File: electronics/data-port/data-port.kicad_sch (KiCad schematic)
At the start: 0 parts

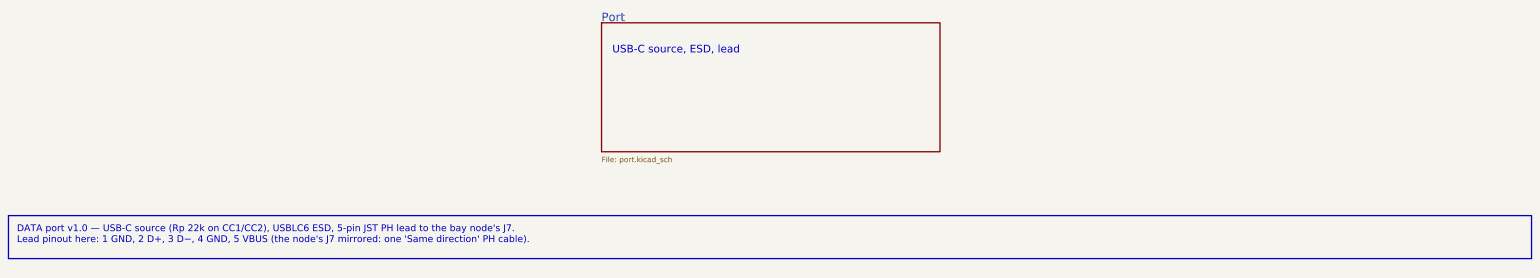
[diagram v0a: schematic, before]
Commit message: DATA lead on 8 wires: node J7 a vertical PH 8 (USB, I²C, INT), data port J2 an S8B
Density decisions of 2026-10-19: the DATA lead becomes the camera's PH 8
"Same direction" type and also carries the node's I²C and an open-drain,
active-low INT (IO4, 10k pull-up, 1k at J7) for a later DATA ×4 board.

- Node: J7 B8B vertical by the right edge (J5's old slot), J5 AUX
  horizontal in the middle, AUX parts in a column between them.  J7 now
  taps the pair at J4's pads (DUT_CONN_*, behind U8's ESD like J4); the
  branch is hand-drawn in usb_hs_routes() on B.Cu under J4, since
  Freerouting found no room on U8's mux side.  ERC 0, DRC 0, parity 0,
  99 models.
- Data port: S8B, pins 1–3 open, PH at x 14.4, left hole (2.6, 13.5),
  one silkscreen label per pin.  ERC 0, DRC 0, parity 0.
- Pin map (README, check_pinmap: DATA_INT reserved), docs, cabling,
  BOM (one PH 8 lead type for DATA and camera, no B5B/S5B), SCAD config.

Co-Authored-By: Claude Opus 5.5 <noreply@anthropic.com>
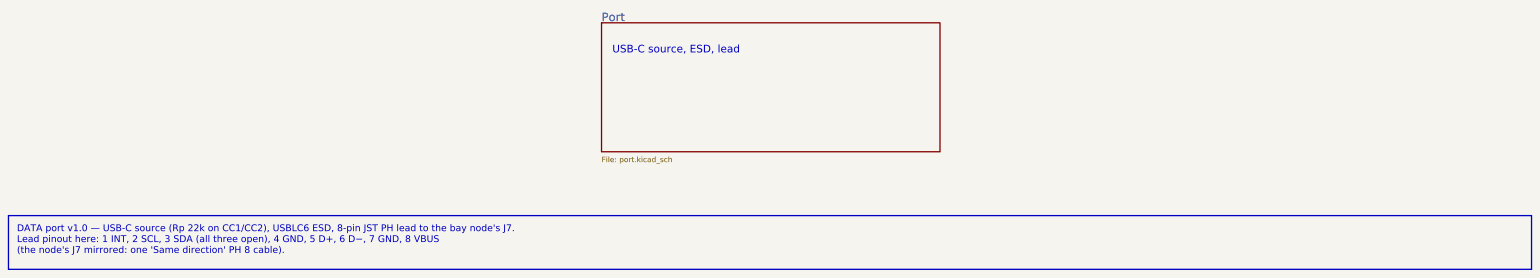
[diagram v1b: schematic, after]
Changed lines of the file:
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@@
 		)
 	)
-	(text_box "DATA port v1.0 — USB-C source (Rp 22k on CC1/CC2), USBLC6 ESD, 5-pin JST PH lead to the bay node's J7.\nLead pinout here: 1 GND, 2 D+, 3 D−, 4 GND, 5 VBUS (the node's J7 mirrored: one 'Same direction' PH cable)."
+	(text_box "DATA port v1.0 — USB-C source (Rp 22k on CC1/CC2), USBLC6 ESD, 8-pin JST PH lead to the bay node's J7.\nLead pinout here: 1 INT, 2 SCL, 3 SDA (all three open), 4 GND, 5 D+, 6 D−, 7 GND, 8 VBUS\n  (the node's J7 mirrored: one 'Same direction' PH 8 cable)."
 		(exclude_from_sim no)
 		(at 30 115.57 0)
-		(size 360 10.16)
+		(size 360 12.7)
 		(margins 2 2 2 2)
 		(stroke

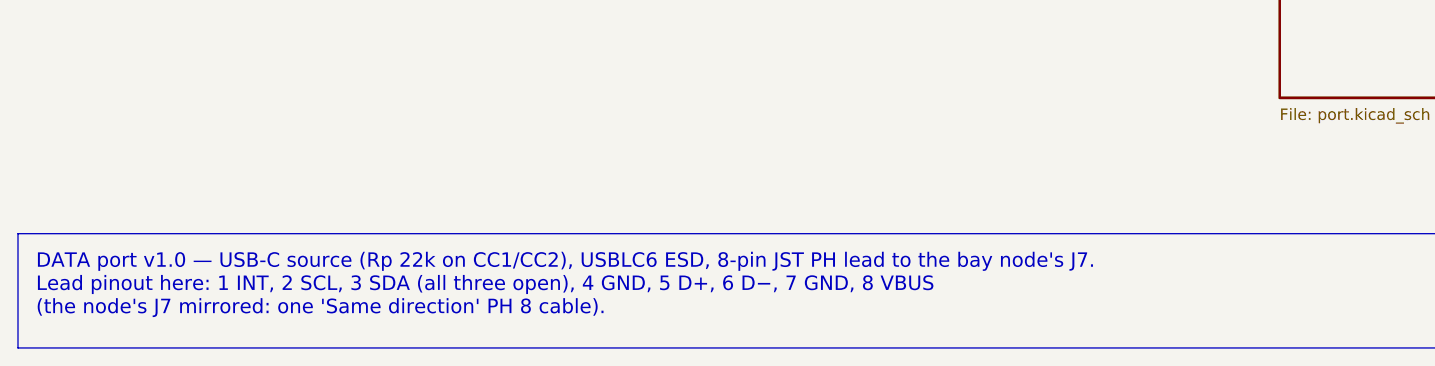
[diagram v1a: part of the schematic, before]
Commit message: Bay node: J7 takes D+ on pin 3, the DUT pair runs straight
U8 puts D- to the north and J7's side entry put D+ there, so D+ crossed
under D- on B.Cu.  The user chose to swap J7's pins 3/4 (3 D+, 4 D-):
DUT_CONN_DP/DN now run straight from U8 into J7, one 45° step each, no
via (14.6 / 14.7 mm; J3 -> J7 matched to ≈ 0.3 mm).

The data port follows through the lead (pin n <-> 9-n): J2 5 D-, 6 D+,
and U1's channels swap with it (D+ through 1/6), so every pad keeps the
copper it had.  Both boards re-routed: ERC 0, DRC 0, 0 unconnected,
parity 0, JLC READY.

The node's buck GND and +5V islands and the LDO tab are now exclusive
(0.5 mm), as on the hub: Freerouting cut buck-5v, then C12 off the LDO
tab.  Docs: electronics (HS path, J7 and lead pinouts), cabling, the
third Konnect round; BOM note.

Co-Authored-By: Claude Opus 5.5 <noreply@anthropic.com>
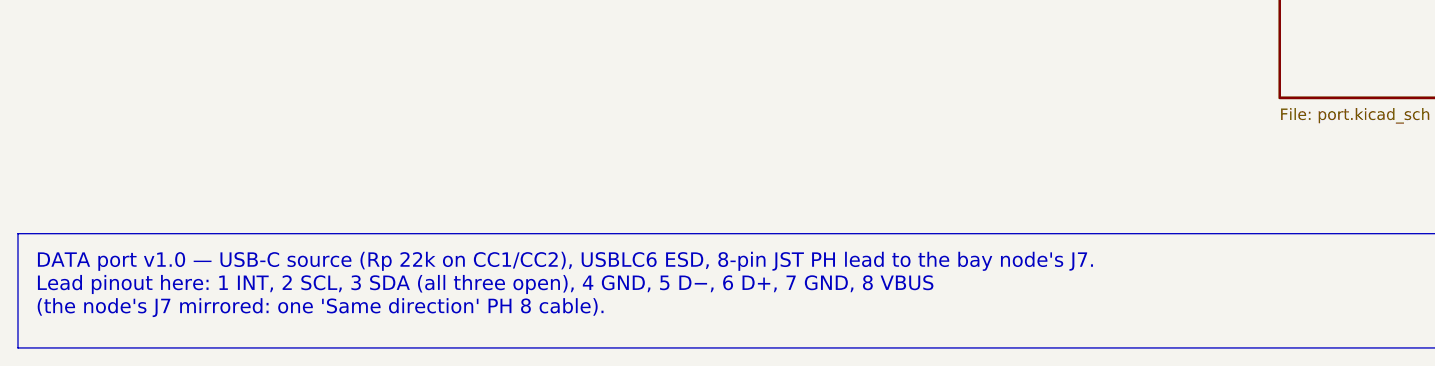
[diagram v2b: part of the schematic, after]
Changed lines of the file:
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@@
 		)
 	)
-	(text_box "DATA port v1.0 — USB-C source (Rp 22k on CC1/CC2), USBLC6 ESD, 8-pin JST PH lead to the bay node's J7.\nLead pinout here: 1 INT, 2 SCL, 3 SDA (all three open), 4 GND, 5 D+, 6 D−, 7 GND, 8 VBUS\n  (the node's J7 mirrored: one 'Same direction' PH 8 cable)."
+	(text_box "DATA port v1.0 — USB-C source (Rp 22k on CC1/CC2), USBLC6 ESD, 8-pin JST PH lead to the bay node's J7.\nLead pinout here: 1 INT, 2 SCL, 3 SDA (all three open), 4 GND, 5 D−, 6 D+, 7 GND, 8 VBUS\n  (the node's J7 mirrored: one 'Same direction' PH 8 cable)."
 		(exclude_from_sim no)
 		(at 30 115.57 0)

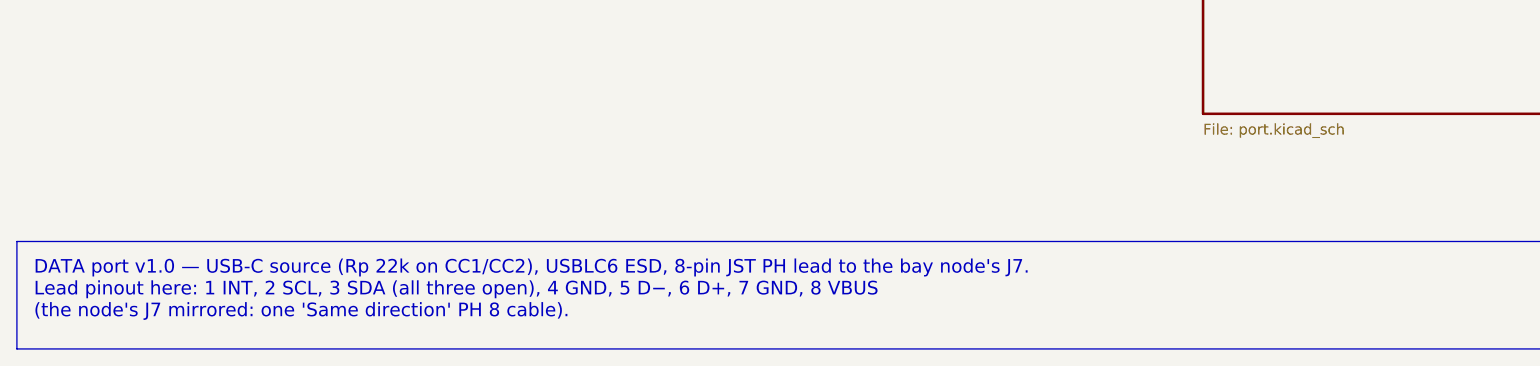
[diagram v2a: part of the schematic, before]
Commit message: DATA port: the PCBA review's fixes
D1: VBUS drawn, 0.8 mm F.Cu from J2.8 under the PH's housing into both of
J1's VBUS pad pairs, necked to 0.5 mm at the pad row (about 15 mOhm
instead of the routed 0.25 mm's 0.13 Ohm), in a Power netclass; thin
tracks to the Rp, C1 and the ESD's VBUS pin.  D2: 10 uF 0805 at the
receptacle (C2, a basic part).  D3: Rp 56k, "default USB power" as on
the DATA x4: 22k would advertise 1.5 A, above the node's TPS2553D low
end of 1.34 A.  D4: a meter check of each PH 8 lead in assembly.md.  D5:
checked in SolidCraft on B-rep (port wall with its U, board, USB4105, a
largest-size plug overmold): the mouth's 0.28 mm overhang sits inside
the U, 2.2 mm clear each side; the overmold clears it by 0.2 mm.

The CPL audit agrees on all 7 parts.  ERC 0, DRC 0, parity 0, 0
unconnected; the BOM follows.

Co-Authored-By: Claude Opus 5.5 <noreply@anthropic.com>
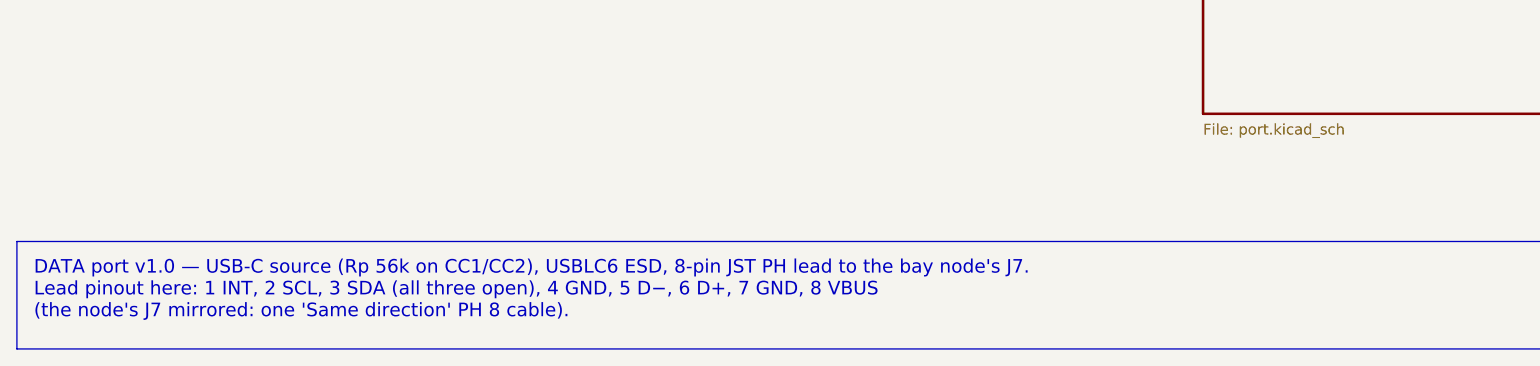
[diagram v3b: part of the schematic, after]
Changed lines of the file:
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@@
 		)
 	)
-	(text_box "DATA port v1.0 — USB-C source (Rp 22k on CC1/CC2), USBLC6 ESD, 8-pin JST PH lead to the bay node's J7.\nLead pinout here: 1 INT, 2 SCL, 3 SDA (all three open), 4 GND, 5 D−, 6 D+, 7 GND, 8 VBUS\n  (the node's J7 mirrored: one 'Same direction' PH 8 cable)."
+	(text_box "DATA port v1.0 — USB-C source (Rp 56k on CC1/CC2), USBLC6 ESD, 8-pin JST PH lead to the bay node's J7.\nLead pinout here: 1 INT, 2 SCL, 3 SDA (all three open), 4 GND, 5 D−, 6 D+, 7 GND, 8 VBUS\n  (the node's J7 mirrored: one 'Same direction' PH 8 cable)."
 		(exclude_from_sim no)
 		(at 30 115.57 0)
